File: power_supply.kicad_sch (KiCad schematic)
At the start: 31 parts, among them U1 2.2uH

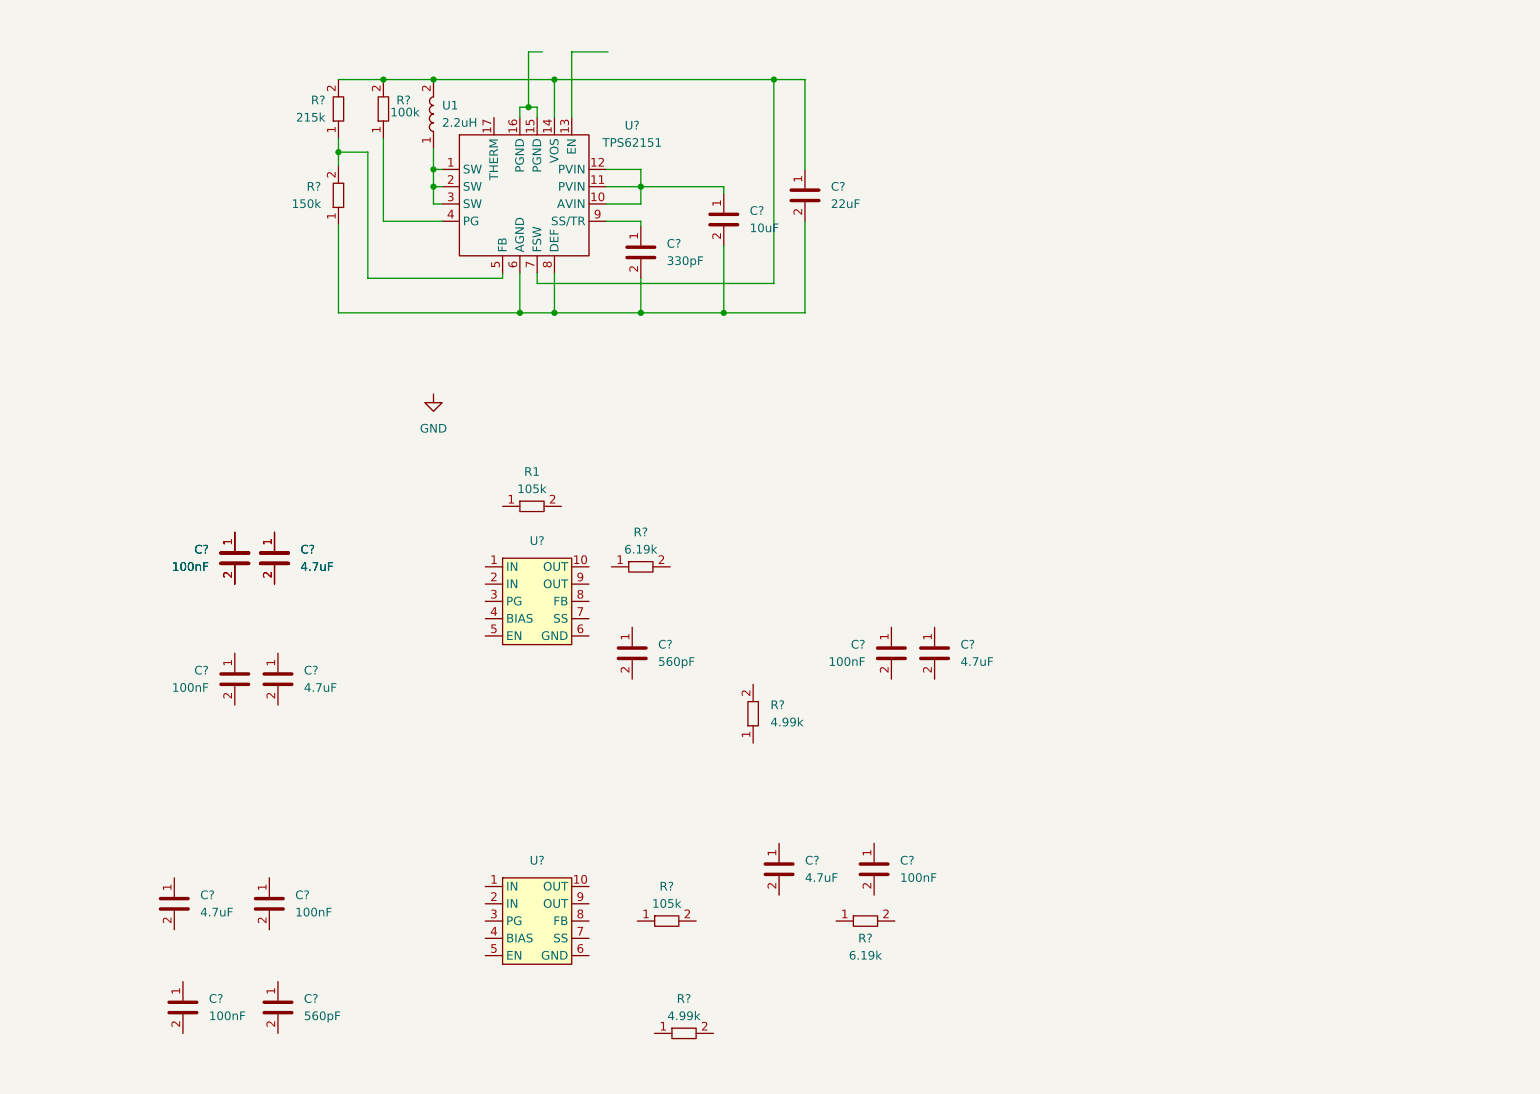
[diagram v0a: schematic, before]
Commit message: Schaltplan für Spannungsversorgung angelegt.
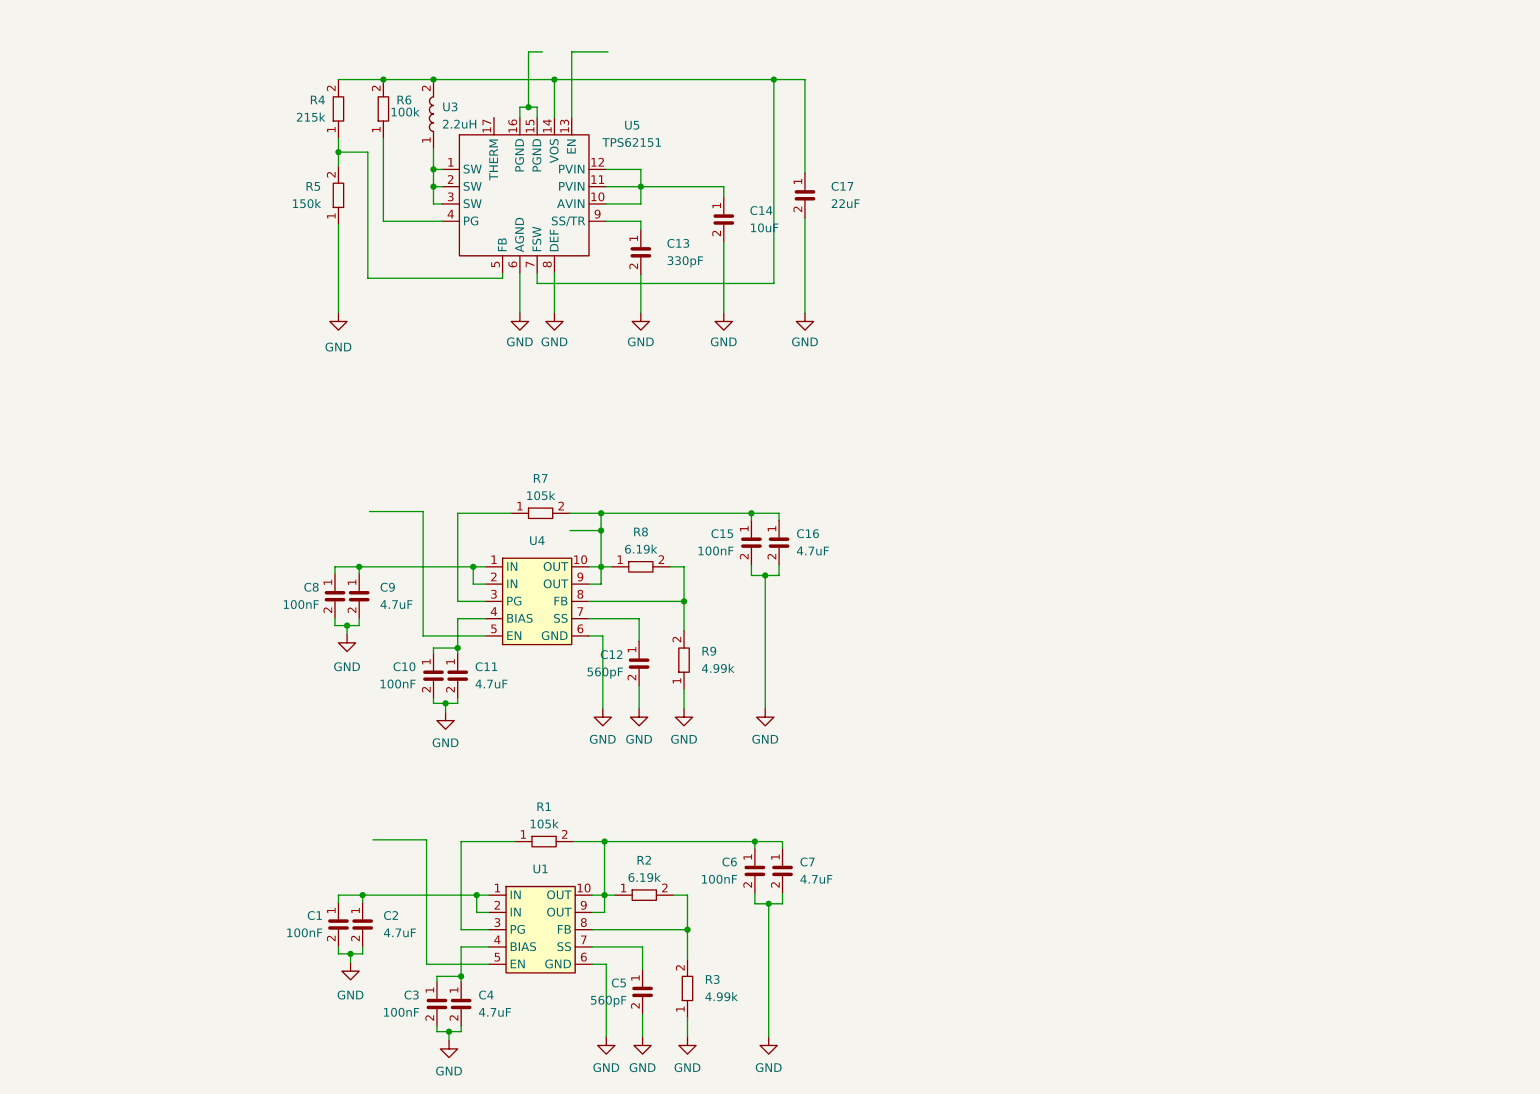
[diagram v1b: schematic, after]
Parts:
- removed C? (x4): C0402_100nF_50V, Capacitor_SMD:C_0402_1005Metric, symbol Jojos_Lib:C0402_100nF_50V
- removed C? (x3): C0402_4.7uF_6.3V, Capacitor_SMD:C_0402_1005Metric, symbol Jojos_Lib:C0402_4.7uF_6.3V
- removed C?: C0402_560p_10V, Capacitor_SMD:C_0402_1005Metric, symbol Jojos_Lib:C0402_560pF_10V
- removed R?: R0402_4.99k, Resistor_SMD:R_0402_1005Metric, symbol Jojos_Lib:R0402_4.99k
- removed R?: R0402_105k, Resistor_SMD:R_0402_1005Metric, symbol Jojos_Lib:R0402_105k
- removed R?: R0402_6.19k, Resistor_SMD:R_0402_1005Metric, symbol Jojos_Lib:R0402_6.19k
- removed U?: ~, Package_SON:VSON-10-1EP_3x3mm_P0.5mm_EP1.65x2.4mm, symbol Jojos_Lib:TPS74801DRCR
- added C1, C3, C6: C0402_100nF_50V, Capacitor_SMD:C_0402_1005Metric, symbol Jojos_Lib:C0402_100nF_50V
- added C2, C4, C7: C0402_4.7uF_6.3V, Capacitor_SMD:C_0402_1005Metric, symbol Jojos_Lib:C0402_4.7uF_6.3V
- added C5: C0402_560p_10V, Capacitor_SMD:C_0402_1005Metric, symbol Jojos_Lib:C0402_560pF_10V
- added R1: R0402_105k, Resistor_SMD:R_0402_1005Metric, symbol Jojos_Lib:R0402_105k
- added R2: R0402_6.19k, Resistor_SMD:R_0402_1005Metric, symbol Jojos_Lib:R0402_6.19k
- added R3: R0402_4.99k, Resistor_SMD:R_0402_1005Metric, symbol Jojos_Lib:R0402_4.99k
- added U1: ~, Package_SON:VSON-10-1EP_3x3mm_P0.5mm_EP1.65x2.4mm, symbol Jojos_Lib:TPS74801DRCR
- gave numbers to parts that had none: 17
- renumbered R1 to R7, U1 to U3
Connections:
- net GND: now also C10.2, C11.2, C12.2, C13.2, C14.2, C15.2, C16.2, C17.2, C8.2, C9.2, R5.1, R9.1, U4.6 (GND), U5.6 (AGND), U5.8 (DEF), C1.2, C2.2, C3.2, C4.2, C5.2, C6.2, C7.2, R3.1, U1.6 (GND)
- net at R8.1: now also C15.1, C16.1, R7.2, U4.10 (OUT), U4.9 (OUT)
- net at R8.2: now also R9.2, U4.8 (FB)
- net at C8.1: now also C9.1, U4.1 (IN), U4.2 (IN)
- net at R7.1: now also U4.3 (PG)
- net at C10.1: now also C11.1, U4.4 (BIAS)
- net at U4.7 (SS): now also C12.1
- new net: C1.1, C2.1, U1.1 (IN), U1.2 (IN)
- new net: C6.1, C7.1, R1.2, R2.1, U1.10 (OUT), U1.9 (OUT)
- new net: R1.1, U1.3 (PG)
- new net: C3.1, C4.1, U1.4 (BIAS)
- new net: C5.1, U1.7 (SS)
- new net: R2.2, R3.2, U1.8 (FB)
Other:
- moved on the sheet: C10, C11, C12, C15, C16, C8, C9, R7, R9

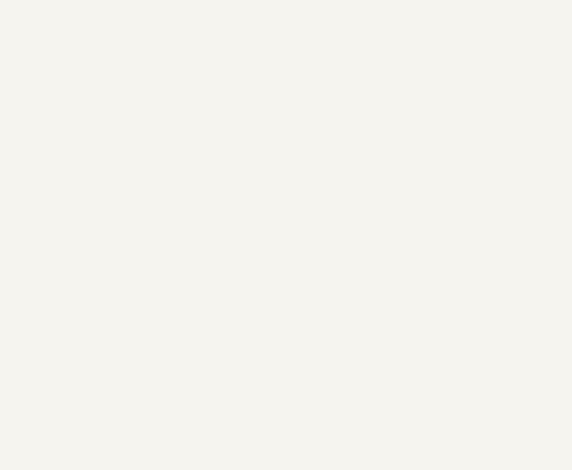
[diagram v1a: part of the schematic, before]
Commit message: Added awags and dac sheet.
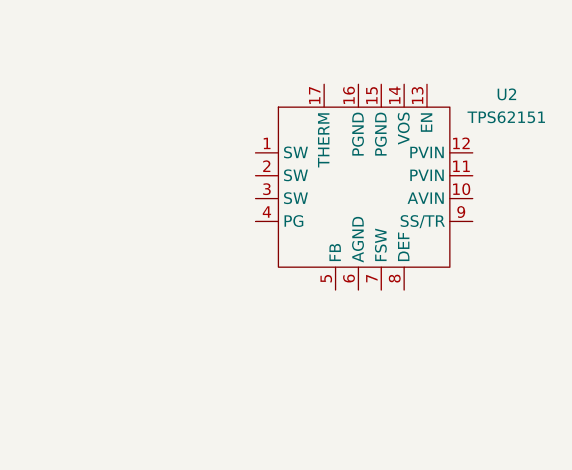
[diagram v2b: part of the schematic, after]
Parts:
- added U2: TPS62151, Package_DFN_QFN:VQFN-16-1EP_3x3mm_P0.5mm_EP1.68x1.68mm, symbol Jojos_Lib:TPS62151
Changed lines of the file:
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@@
+    )
+  )
+  (symbol (lib_id "Jojos_Lib:TPS62151") (at 222.25 37.084 0) (unit 1)
+    (in_bom yes) (on_board yes) (dnp no) (fields_autoplaced)
+    (property "Reference" "U2" (at 237.49 25.5523 0)
+      (effects (font (size 1.27 1.27)))
+    )
+    (property "Value" "TPS62151" (at 237.49 28.0923 0)
+      (effects (font (size 1.27 1.27)))
+    )
+    (property "Footprint" "Package_DFN_QFN:VQFN-16-1EP_3x3mm_P0.5mm_EP1.68x1.68mm" (at 224.79 42.164 0)
+      (effects (font (size 1.27 1.27)) hide)
+    )
+    (property "Datasheet" "" (at 224.79 42.164 0)
+      (effects (font (size 1.27 1.27)) hide)
+    )
+    (property "Mouser Part Number" "595-TPS62150RGTR " (at 222.25 37.084 0)
+      (effects (font (size 1.27 1.27)) hide)
+    )
+    (property "Place" "yes" (at 222.25 37.084 0)
+      (effects (font (size 1.27 1.27)) hide)
+    )
+    (pin "1")
+    (pin "10")
+    (pin "11")
+    (pin "12")
+    (pin "13")
+    (pin "14")
+    (pin "15")
+    (pin "16")
+    (pin "17")
+    (pin "2")
+    (pin "3")
+    (pin "4")
+    (pin "5")
+    (pin "6")
+    (pin "7")
+    (pin "8")
+    (pin "9")
+    (instances
+      (project "CMEX"
+        (path "/03c4a148-37f4-4d5a-ada3-efb0d725ba7b"
+          (reference "U2") (unit 1)
+        )
+        (path "/03c4a148-37f4-4d5a-ada3-efb0d725ba7b/c5d85882-7f42-4413-996b-8b864785f647"
+          (reference "U2") (unit 1)
+        )
+      )
     )
   )

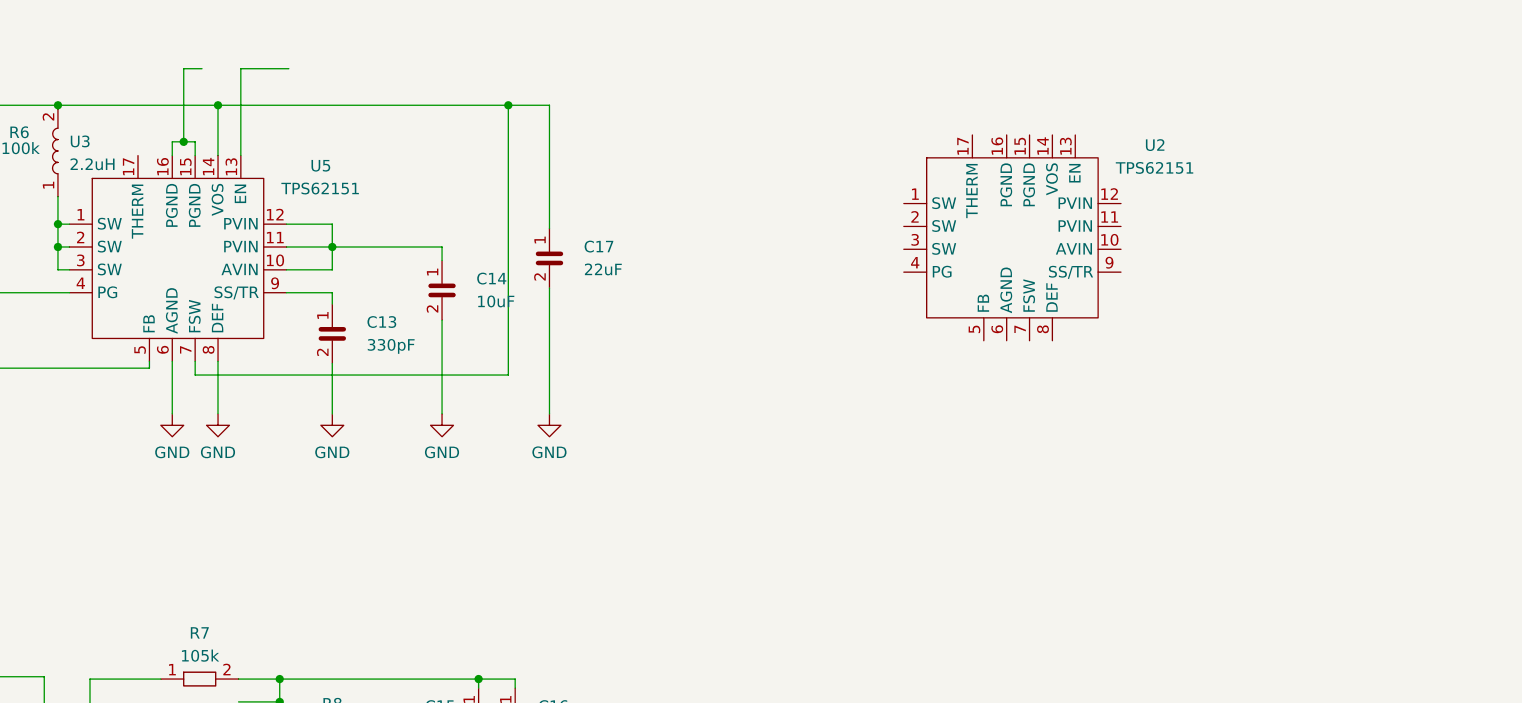
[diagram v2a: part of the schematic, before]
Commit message: Changed power supply.
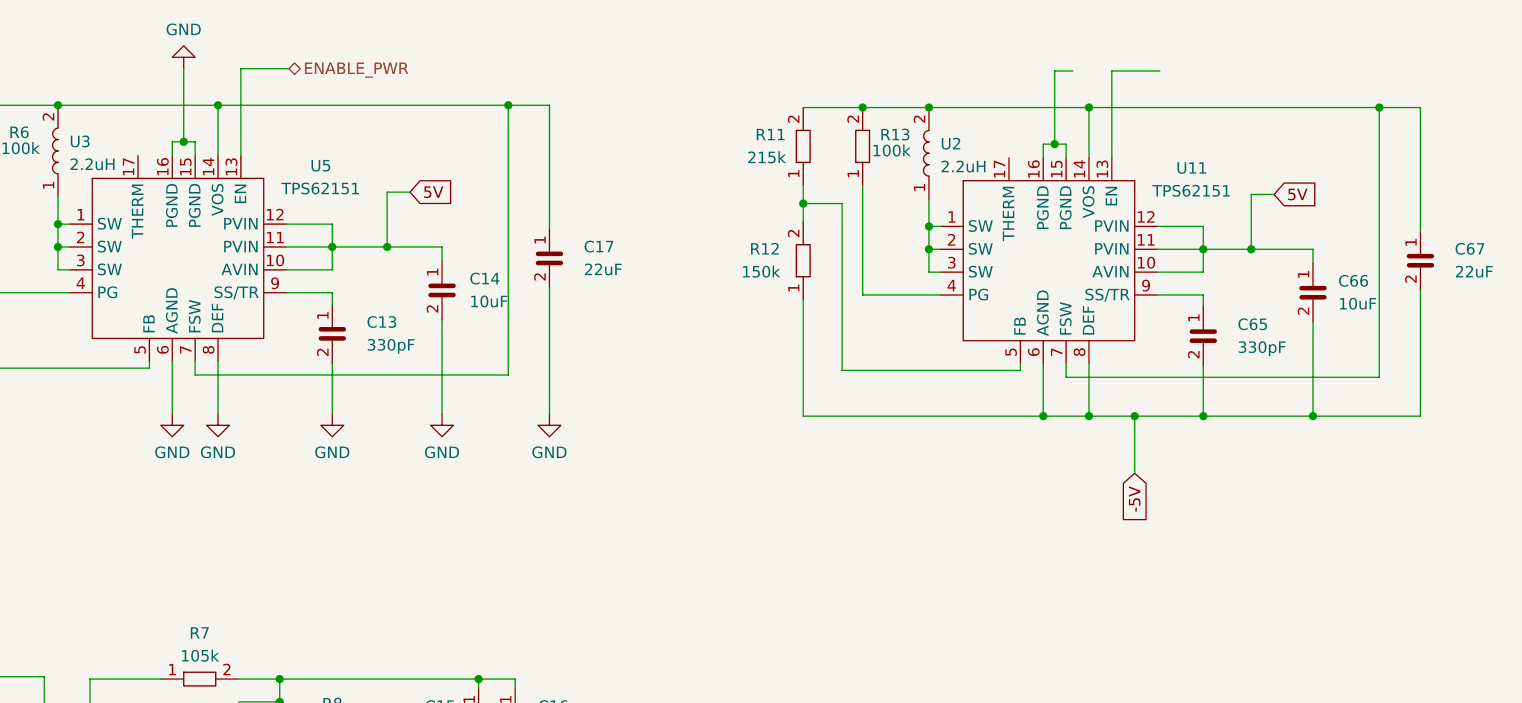
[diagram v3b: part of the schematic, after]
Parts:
- removed U2: TPS62151, Package_DFN_QFN:VQFN-16-1EP_3x3mm_P0.5mm_EP1.68x1.68mm, symbol Jojos_Lib:TPS62151
- added C65: C0402_330p_25V, Capacitor_SMD:C_0402_1005Metric, symbol Jojos_Lib:C0402_330pF_25V
- added C66: C0402_10uF_6.3V, Capacitor_SMD:C_0402_1005Metric, symbol Jojos_Lib:C0402_10uF_6.3V
- added C67: C0402_22uF_6.3V, Capacitor_SMD:C_0402_1005Metric, symbol Jojos_Lib:C0402_22uF_6.3V
- added R11: R0402_215k, Resistor_SMD:R_0402_1005Metric, symbol Jojos_Lib:R0402_215k
- added R12: R0402_150k, Resistor_SMD:R_0402_1005Metric, symbol Jojos_Lib:R0402_150k
- added R13: R0402_100k, Resistor_SMD:R_0402_1005Metric, symbol Jojos_Lib:R0402_100k
- added U11: TPS62151, Package_DFN_QFN:VQFN-16-1EP_3x3mm_P0.5mm_EP1.68x1.68mm, symbol Jojos_Lib:TPS62151
- added U2: 2.2uH, Inductor_SMD:L_Coilcraft_XAL60xx_6.36x6.56mm, symbol Jojos_Lib:L2.2uH
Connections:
- net GND: now also U5.15 (PGND), U5.16 (PGND)
- net 5V: now reaches C14.1, U5.10 (AVIN), U5.11 (PVIN), U5.12 (PVIN)
- net 5V: now also C66.1, U11.10 (AVIN), U11.11 (PVIN), U11.12 (PVIN)
- net ENABLE_PWR: now reaches U5.13 (EN)
- new net: R11.1, R12.2, U11.5 (FB)
- new net: C67.1, R11.2, R13.2, U11.14 (VOS), U11.7 (FSW), U2.2
- new net: U11.1 (SW), U11.2 (SW), U11.3 (SW), U2.1
- new net: U11.15 (PGND), U11.16 (PGND)
- new net: R13.1, U11.4 (PG)
- new net: C65.1, U11.9 (SS/TR)
- new net -5V: C65.2, C66.2, C67.2, R12.1, U11.6 (AGND), U11.8 (DEF)

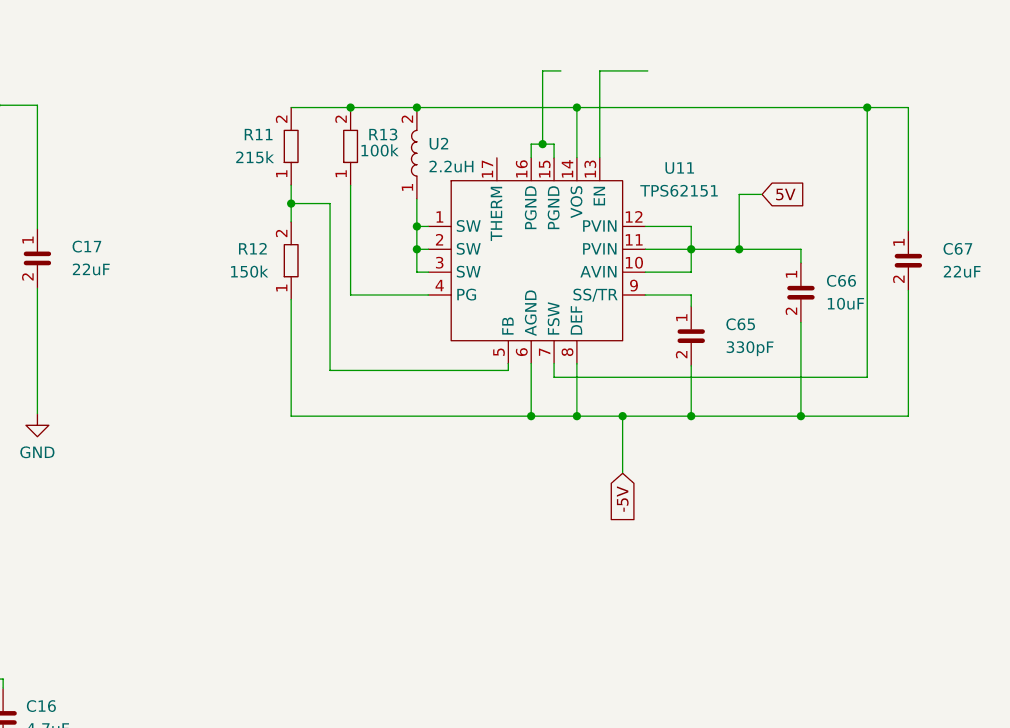
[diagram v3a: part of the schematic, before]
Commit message: Added negative power supply.
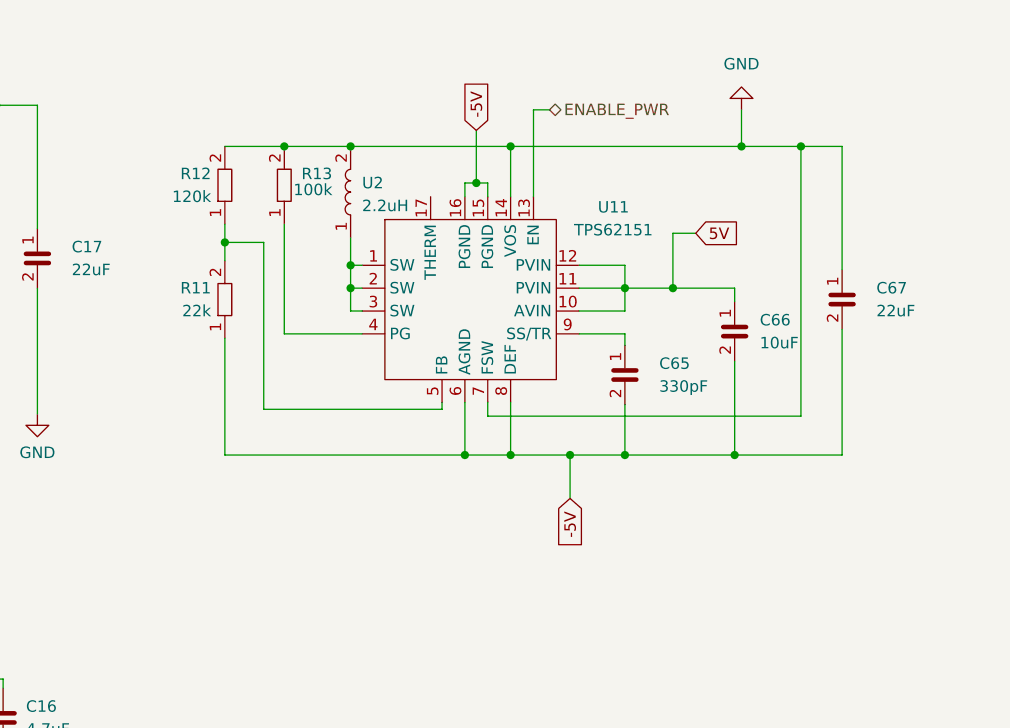
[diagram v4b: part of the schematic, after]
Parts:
- removed R11: R0402_215k, Resistor_SMD:R_0402_1005Metric, symbol Jojos_Lib:R0402_215k
- removed R12: R0402_150k, Resistor_SMD:R_0402_1005Metric, symbol Jojos_Lib:R0402_150k
- added R11: R0402_22k, Resistor_SMD:R_0402_1005Metric, symbol Jojos_Lib:R0402_22k
- added R12: R0402_120k, Resistor_SMD:R_0402_1005Metric, symbol Jojos_Lib:R0402_120k
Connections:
- net -5V: now also U11.15 (PGND), U11.16 (PGND), R11.1
- net ENABLE_PWR: now also U11.13 (EN)
- net GND: now also C67.1, R13.2, U11.14 (VOS), U11.7 (FSW), U2.2, R12.2
- net at U11.5 (FB): now also R11.2, R12.1
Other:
- moved on the sheet: C65, C66, C67, R13, U11, U2
